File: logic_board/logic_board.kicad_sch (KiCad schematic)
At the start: 1 part

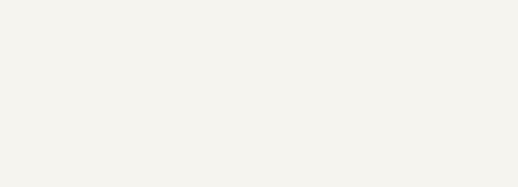
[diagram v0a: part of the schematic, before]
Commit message: Add headphone jack
Change PCB to proper size.
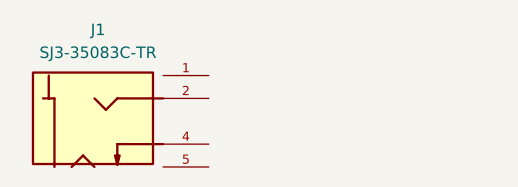
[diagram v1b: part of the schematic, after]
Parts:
- added J1: SJ3-35083C-TR, Custom_Footprints:SAMESKY_SJ3-35083C-TR, symbol Custom_Symbols:SJ3-35083C-TR
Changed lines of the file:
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@@
 	(paper "A4")
+	(symbol
+		(lib_id "Custom_Symbols:SJ3-35083C-TR")
+		(at 73.66 96.52 0)
+		(unit 1)
+		(exclude_from_sim no)
+		(in_bom yes)
+		(on_board yes)
+		(dnp no)
+		(fields_autoplaced yes)
+		(property "Reference" "J1"
+			(at 71.5134 86.36 0)
+			(effects
+				(font
+					(size 1.27 1.27)
+				)
+			)
+		)
+		(property "Value" "SJ3-35083C-TR"
+			(at 71.5134 88.9 0)
+			(effects
+				(font
+					(size 1.27 1.27)
+				)
+			)
+		)
+		(property "Footprint" "Custom_Footprints:SAMESKY_SJ3-35083C-TR"
+			(at 73.66 96.52 0)
+			(effects
+				(font
+					(size 1.27 1.27)
+				)
+				(justify bottom)
+				(hide yes)
+			)
+		)
+		(property "Datasheet" "https://www.sameskydevices.com/product/resource/sj3-3508x.pdf"
+			(at 73.66 96.52 0)
+			(effects
+				(font
+					(size 1.27 1.27)
+				)
+				(hide yes)
+			)
+		)
+		(property "Description" "3.5mm Audio Jack"
+			(at 73.66 96.52 0)
+			(effects
+				(font
+					(size 1.27 1.27)
+				)
+				(hide yes)
+			)
+		)
+		(property "PARTREV" "1.01"
+			(at 73.66 96.52 0)
+			(effects
+				(font
+					(size 1.27 1.27)
+				)
+				(justify bottom)
+				(hide yes)
+			)
+		)
+		(property "STANDARD" "Manufacturer Recommendations"
+			(at 73.66 96.52 0)
+			(effects
+				(font
+					(size 1.27 1.27)
+				)
+				(justify bottom)
+				(hide yes)
+			)
+		)
+		(property "MAXIMUM_PACKAGE_HEIGHT" "5.3mm"
+			(at 73.66 96.52 0)
+			(effects
+				(font
+					(size 1.27 1.27)
+				)
+				(justify bottom)
+				(hide yes)
+			)
+		)
+		(property "MANUFACTURER" "Same Sky"
+			(at 73.66 96.52 0)
+			(effects
+				(font
+					(size 1.27 1.27)
+				)
+				(justify bottom)
+				(hide yes)
+			)
+		)
+		(pin "1"
+		)
+		(pin "2"
+		)
+		(pin "4"
+		)
+		(pin "5"
+		)
+		(instances
+			(project ""
+				(path "/b7b37fe1-b409-497a-9440-d94d882f6459"
+					(reference "J1")
+					(unit 1)
+				)
+			)
+		)
+	)
 	(symbol
 		(lib_id "Device:R")

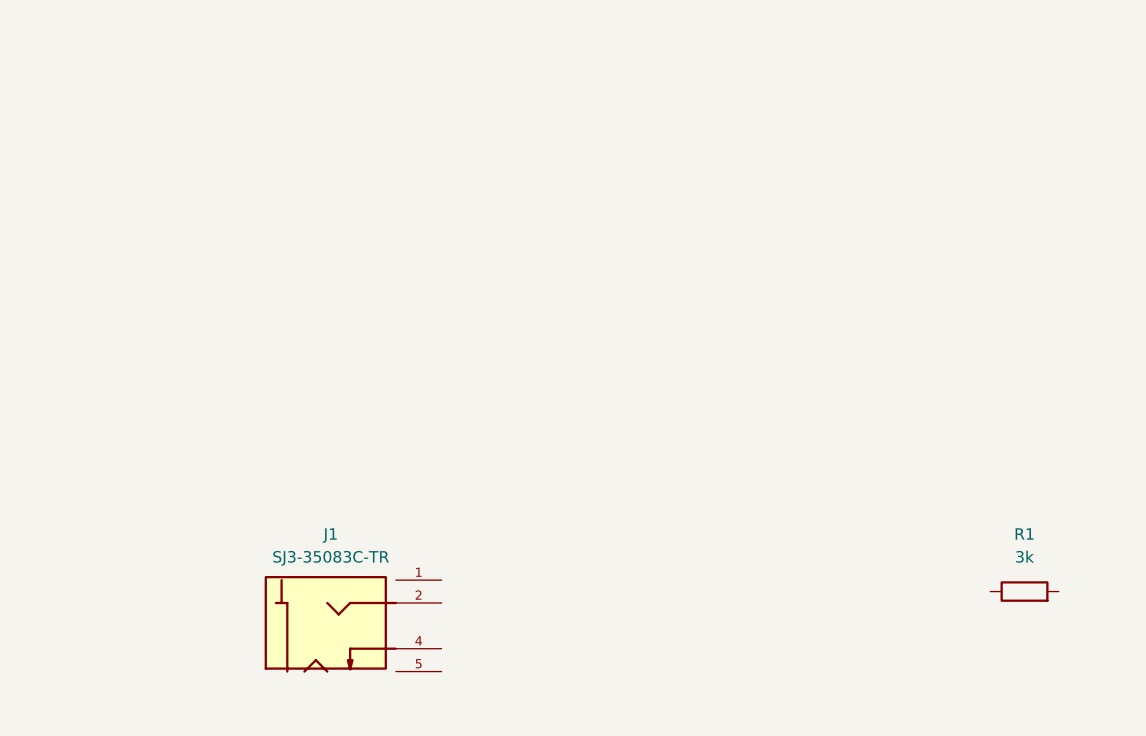
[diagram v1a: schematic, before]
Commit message: Component selection
Imported specific parts into KiCAD project library (including JLCPCB part numbers).
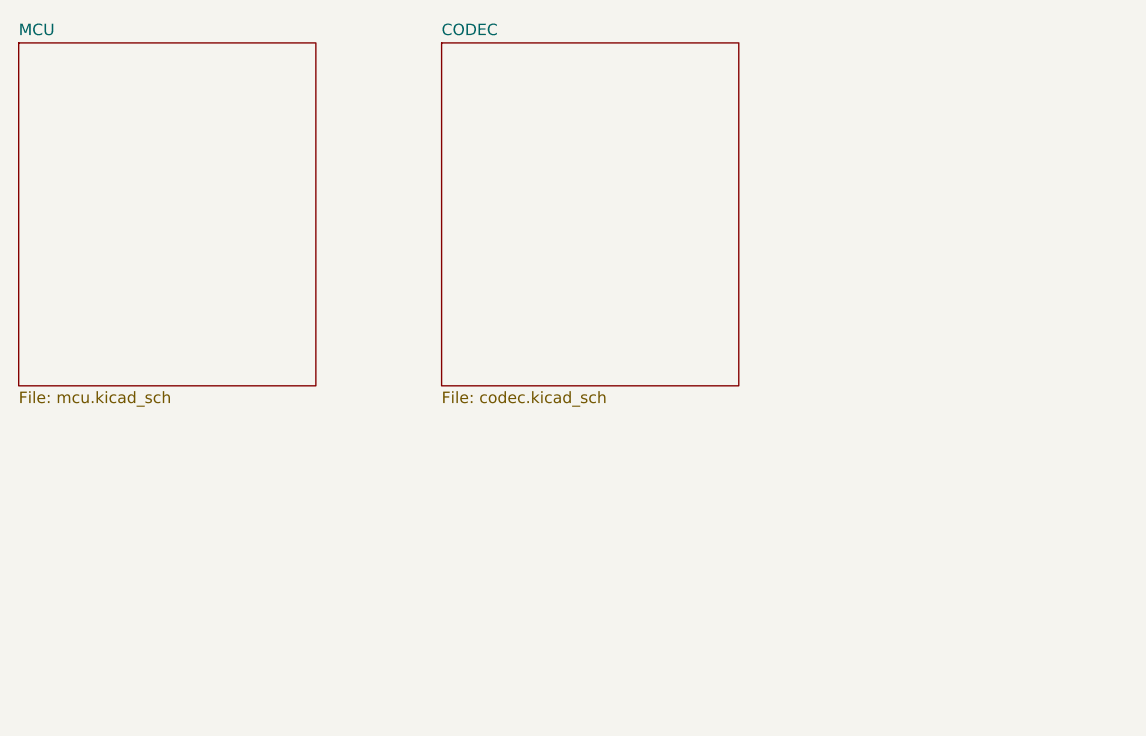
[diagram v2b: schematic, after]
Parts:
- removed J1: SJ3-35083C-TR, Custom_Footprints:SAMESKY_SJ3-35083C-TR, symbol Custom_Symbols:SJ3-35083C-TR
- removed R1: 3k, Resistor_SMD:R_0402_1005Metric, symbol Device:R
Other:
- added sheet CODEC (codec.kicad_sch)
- added sheet MCU (mcu.kicad_sch)
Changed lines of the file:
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@@
 	(generator_version "9.0")
 	(paper "A4")
-	(symbol
-		(lib_id "Custom_Symbols:SJ3-35083C-TR")
-		(at 73.66 96.52 0)
-		(unit 1)
+	(sheet
+		(at 83.82 31.75)
+		(size 33.02 38.1)
 		(exclude_from_sim no)
 		(in_bom yes)
@@
 		(dnp no)
 		(fields_autoplaced yes)
-		(property "Reference" "J1"
-			(at 71.5134 86.36 0)
+		(stroke
+			(width 0.1524)
+			(type solid)
+		)
+		(fill
+			(color 0 0 0 0.0000)
+		)
+		(property "Sheetname" "CODEC"
+			(at 83.82 31.0384 0)
 			(effects
 				(font
 					(size 1.27 1.27)
 				)
+				(justify left bottom)
 			)
 		)
-		(property "Value" "SJ3-35083C-TR"
-			(at 71.5134 88.9 0)
+		(property "Sheetfile" "codec.kicad_sch"
+			(at 83.82 70.4346 0)
 			(effects
 				(font
 					(size 1.27 1.27)
 				)
+				(justify left top)
 			)
 		)
-		(property "Footprint" "Custom_Footprints:SAMESKY_SJ3-35083C-TR"
-			(at 73.66 96.52 0)
-			(effects
-				(font
-					(size 1.27 1.27)
-				)
-				(justify bottom)
-				(hide yes)
-			)
-		)
-		(property "Datasheet" "https://www.sameskydevices.com/product/resource/sj3-3508x.pdf"
-			(at 73.66 96.52 0)
-			(effects
-				(font
-					(size 1.27 1.27)
-				)
-				(hide yes)
-			)
-		)
-		(property "Description" "3.5mm Audio Jack"
-			(at 73.66 96.52 0)
-			(effects
-				(font
-					(size 1.27 1.27)
-				)
-				(hide yes)
-			)
-		)
-		(property "PARTREV" "1.01"
-			(at 73.66 96.52 0)
-			(effects
-				(font
-					(size 1.27 1.27)
-				)
-				(justify bottom)
-				(hide yes)
-			)
-		)
-		(property "STANDARD" "Manufacturer Recommendations"
-			(at 73.66 96.52 0)
-			(effects
-				(font
-					(size 1.27 1.27)
-				)
-				(justify bottom)
-				(hide yes)
-			)
-		)
-		(property "MAXIMUM_PACKAGE_HEIGHT" "5.3mm"
-			(at 73.66 96.52 0)
-			(effects
-				(font
-					(size 1.27 1.27)
-				)
-				(justify bottom)
-				(hide yes)
-			)
-		)
-		(property "MANUFACTURER" "Same Sky"
-			(at 73.66 96.52 0)
-			(effects
-				(font
-					(size 1.27 1.27)
-				)
-				(justify bottom)
-				(hide yes)
-			)
-		)
-		(pin "1"
-		)
-		(pin "2"
-		)
-		(pin "4"
-		)
-		(pin "5"
-		)
 		(instances
-			(project ""
+			(project "logic_board"
 				(path "/b7b37fe1-b409-497a-9440-d94d882f6459"
-					(reference "J1")
-					(unit 1)
+					(page "3")
 				)
 			)
 		)
 	)
-	(symbol
-		(lib_id "Device:R")
-		(at 148.59 92.71 90)
-		(unit 1)
+	(sheet
+		(at 36.83 31.75)
+		(size 33.02 38.1)
 		(exclude_from_sim no)
 		(in_bom yes)
@@
 		(dnp no)
 		(fields_autoplaced yes)
-		(property "Reference" "R1"
-			(at 148.59 86.36 90)
+		(stroke
+			(width 0.1524)
+			(type solid)
+		)
+		(fill
+			(color 0 0 0 0.0000)
+		)
+		(property "Sheetname" "MCU"
+			(at 36.83 31.0384 0)
 			(effects
 				(font
 					(size 1.27 1.27)
 				)
+				(justify left bottom)
 			)
 		)
-		(property "Value" "3k"
-			(at 148.59 88.9 90)
+		(property "Sheetfile" "mcu.kicad_sch"
+			(at 36.83 70.4346 0)
 			(effects
 				(font
 					(size 1.27 1.27)
 				)
+				(justify left top)
 			)
 		)
-		(property "Footprint" "Resistor_SMD:R_0402_1005Metric"
-			(at 148.59 94.488 90)
-			(effects
-				(font
-					(size 1.27 1.27)
-				)
-				(hide yes)
-			)
-		)
-		(property "Datasheet" "~"
-			(at 148.59 92.71 0)
-			(effects
-				(font
-					(size 1.27 1.27)
-				)
-				(hide yes)
-			)
-		)
-		(property "Description" "Resistor"
-			(at 148.59 92.71 0)
-			(effects
-				(font
-					(size 1.27 1.27)
-				)
-				(hide yes)
-			)
-		)
-		(property "LCSC Part Number" "C4211"
-			(at 148.59 92.71 90)
-			(effects
-				(font
-					(size 1.27 1.27)
-				)
-				(hide yes)
-			)
-		)
-		(pin "2"
-		)
-		(pin "1"
-		)
 		(instances
-			(project ""
+			(project "logic_board"
 				(path "/b7b37fe1-b409-497a-9440-d94d882f6459"
-					(reference "R1")
-					(unit 1)
+					(page "2")
 				)
 			)

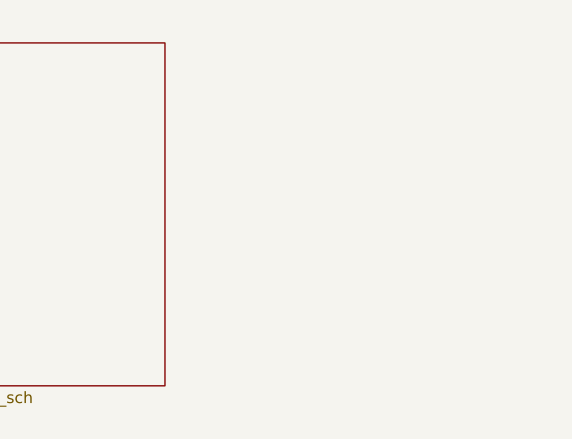
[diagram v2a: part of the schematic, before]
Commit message: Ready for routing. - Lay out all components in proper positions - Add all support passives (bypass caps, etc) - Add board corner cutouts for enclosure bosses.
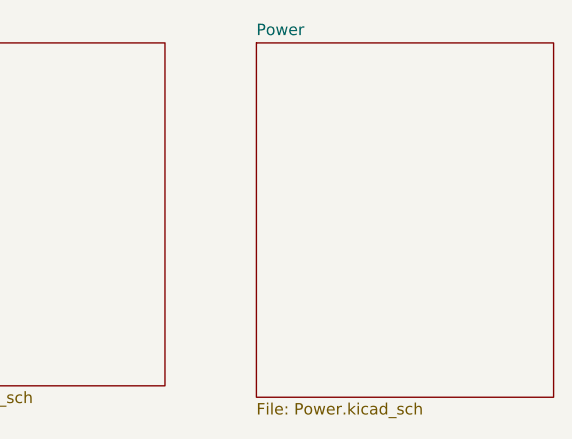
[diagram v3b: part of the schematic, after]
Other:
- added sheet Power (Power.kicad_sch)
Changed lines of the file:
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@@
 	(paper "A4")
+	(sheet
+		(at 127 31.75)
+		(size 33.02 39.37)
+		(exclude_from_sim no)
+		(in_bom yes)
+		(on_board yes)
+		(dnp no)
+		(fields_autoplaced yes)
+		(stroke
+			(width 0.1524)
+			(type solid)
+		)
+		(fill
+			(color 0 0 0 0.0000)
+		)
+		(property "Sheetname" "Power"
+			(at 127 31.0384 0)
+			(effects
+				(font
+					(size 1.27 1.27)
+				)
+				(justify left bottom)
+			)
+		)
+		(property "Sheetfile" "Power.kicad_sch"
+			(at 127 71.7046 0)
+			(effects
+				(font
+					(size 1.27 1.27)
+				)
+				(justify left top)
+			)
+		)
+		(instances
+			(project "logic_board"
+				(path "/b7b37fe1-b409-497a-9440-d94d882f6459"
+					(page "4")
+				)
+			)
+		)
+	)
 	(sheet
 		(at 83.82 31.75)

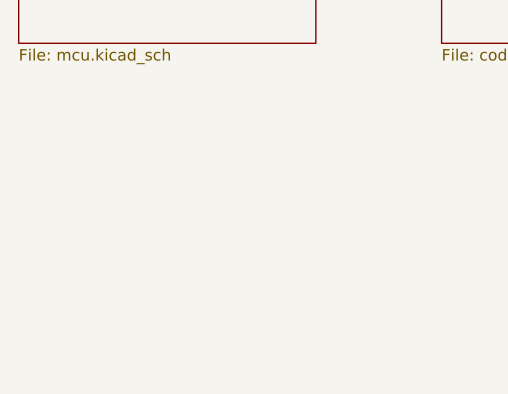
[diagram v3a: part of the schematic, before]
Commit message: Add fiducials take 2
Need to add to schematic so they don't get deleted with updating PCB from
schematic.
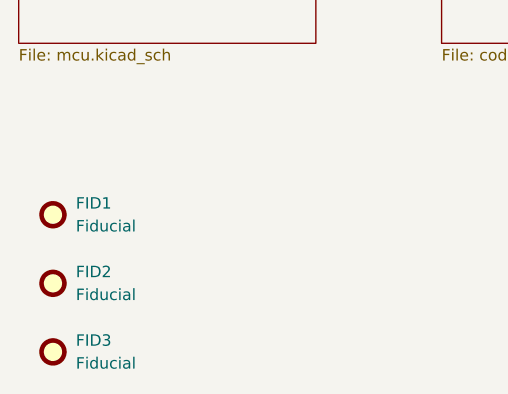
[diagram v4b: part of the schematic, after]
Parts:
- added FID1, FID2, FID3: Fiducial, Fiducial:Fiducial_0.5mm_Mask1mm, symbol Mechanical:Fiducial
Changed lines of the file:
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@@
 	(generator_version "9.0")
 	(paper "A4")
+	(symbol
+		(lib_id "Mechanical:Fiducial")
+		(at 40.64 104.14 0)
+		(unit 1)
+		(exclude_from_sim no)
+		(in_bom no)
+		(on_board yes)
+		(dnp no)
+		(fields_autoplaced yes)
+		(property "Reference" "FID3"
+			(at 43.18 102.8699 0)
+			(effects
+				(font
+					(size 1.27 1.27)
+				)
+				(justify left)
+			)
+		)
+		(property "Value" "Fiducial"
+			(at 43.18 105.4099 0)
+			(effects
+				(font
+					(size 1.27 1.27)
+				)
+				(justify left)
+			)
+		)
+		(property "Footprint" "Fiducial:Fiducial_0.5mm_Mask1mm"
+			(at 40.64 104.14 0)
+			(effects
+				(font
+					(size 1.27 1.27)
+				)
+				(hide yes)
+			)
+		)
+		(property "Datasheet" "~"
+			(at 40.64 104.14 0)
+			(effects
+				(font
+					(size 1.27 1.27)
+				)
+				(hide yes)
+			)
+		)
+		(property "Description" "Fiducial Marker"
+			(at 40.64 104.14 0)
+			(effects
+				(font
+					(size 1.27 1.27)
+				)
+				(hide yes)
+			)
+		)
+		(instances
+			(project "logic_board"
+				(path "/b7b37fe1-b409-497a-9440-d94d882f6459"
+					(reference "FID3")
+					(unit 1)
+				)
+			)
+		)
+	)
+	(symbol
+		(lib_id "Mechanical:Fiducial")
+		(at 40.64 96.52 0)
+		(unit 1)
+		(exclude_from_sim no)
+		(in_bom no)
+		(on_board yes)
+		(dnp no)
+		(fields_autoplaced yes)
+		(property "Reference" "FID2"
+			(at 43.18 95.2499 0)
+			(effects
+				(font
+					(size 1.27 1.27)
+				)
+				(justify left)
+			)
+		)
+		(property "Value" "Fiducial"
+			(at 43.18 97.7899 0)
+			(effects
+				(font
+					(size 1.27 1.27)
+				)
+				(justify left)
+			)
+		)
+		(property "Footprint" "Fiducial:Fiducial_0.5mm_Mask1mm"
+			(at 40.64 96.52 0)
+			(effects
+				(font
+					(size 1.27 1.27)
+				)
+				(hide yes)
+			)
+		)
+		(property "Datasheet" "~"
+			(at 40.64 96.52 0)
+			(effects
+				(font
+					(size 1.27 1.27)
+				)
+				(hide yes)
+			)
+		)
+		(property "Description" "Fiducial Marker"
+			(at 40.64 96.52 0)
+			(effects
+				(font
+					(size 1.27 1.27)
+				)
+				(hide yes)
+			)
+		)
+		(instances
+			(project "logic_board"
+				(path "/b7b37fe1-b409-497a-9440-d94d882f6459"
+					(reference "FID2")
+					(unit 1)
+				)
+			)
+		)
+	)
+	(symbol
+		(lib_id "Mechanical:Fiducial")
+		(at 40.64 88.9 0)
+		(unit 1)
+		(exclude_from_sim no)
+		(in_bom no)
+		(on_board yes)
+		(dnp no)
+		(fields_autoplaced yes)
+		(property "Reference" "FID1"
+			(at 43.18 87.6299 0)
+			(effects
+				(font
+					(size 1.27 1.27)
+				)
+				(justify left)
+			)
+		)
+		(property "Value" "Fiducial"
+			(at 43.18 90.1699 0)
+			(effects
+				(font
+					(size 1.27 1.27)
+				)
+				(justify left)
+			)
+		)
+		(property "Footprint" "Fiducial:Fiducial_0.5mm_Mask1mm"
+			(at 40.64 88.9 0)
+			(effects
+				(font
+					(size 1.27 1.27)
+				)
+				(hide yes)
+			)
+		)
+		(property "Datasheet" "~"
+			(at 40.64 88.9 0)
+			(effects
+				(font
+					(size 1.27 1.27)
+				)
+				(hide yes)
+			)
+		)
+		(property "Description" "Fiducial Marker"
+			(at 40.64 88.9 0)
+			(effects
+				(font
+					(size 1.27 1.27)
+				)
+				(hide yes)
+			)
+		)
+		(instances
+			(project ""
+				(path "/b7b37fe1-b409-497a-9440-d94d882f6459"
+					(reference "FID1")
+					(unit 1)
+				)
+			)
+		)
+	)
 	(sheet
 		(at 127 31.75)

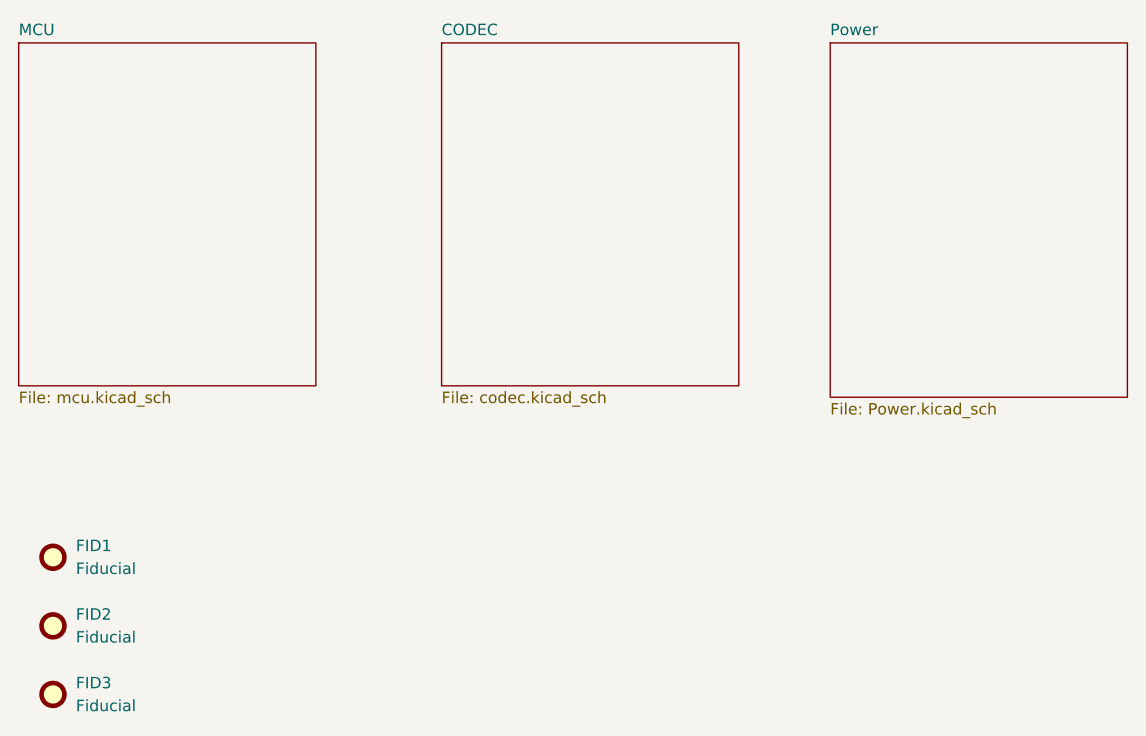
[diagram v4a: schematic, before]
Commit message: Minor cosmetic tweaks, fix silkscreen references
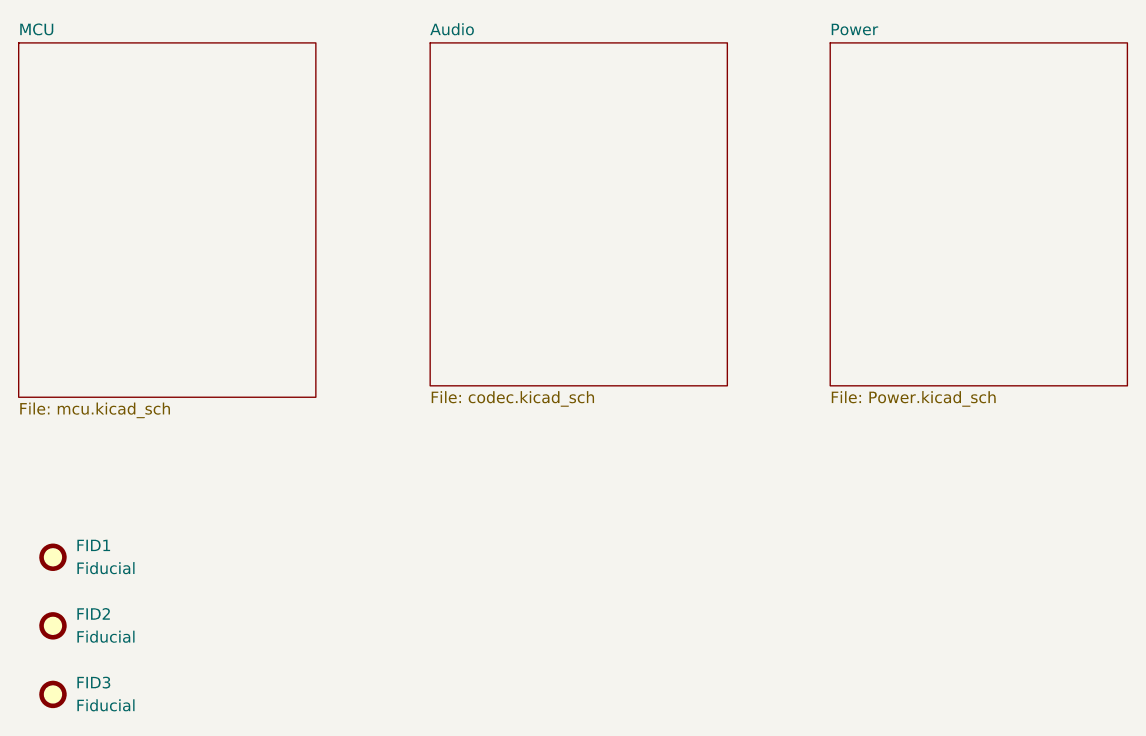
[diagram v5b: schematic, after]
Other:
- sheet CODEC renamed Audio
- title: (none) -> Headphone Guitar Practice Amp
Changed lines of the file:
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@@
 	(generator_version "9.0")
 	(paper "A4")
+	(title_block
+		(title "Headphone Guitar Practice Amp")
+		(date "2026-01-02")
+		(rev "2.0")
+	)
 	(symbol
 		(lib_id "Mechanical:Fiducial")
@@
 	(sheet
 		(at 127 31.75)
-		(size 33.02 39.37)
+		(size 33.02 38.1)
 		(exclude_from_sim no)
 		(in_bom yes)
@@
 		)
 		(property "Sheetfile" "Power.kicad_sch"
-			(at 127 71.7046 0)
+			(at 127 70.4346 0)
 			(effects
 				(font
@@
 	)
 	(sheet
-		(at 83.82 31.75)
+		(at 82.55 31.75)
 		(size 33.02 38.1)
 		(exclude_from_sim no)
@@
 			(color 0 0 0 0.0000)
 		)
-		(property "Sheetname" "CODEC"
-			(at 83.82 31.0384 0)
+		(property "Sheetname" "Audio"
+			(at 82.55 31.0384 0)
 			(effects
 				(font
@@
 		)
 		(property "Sheetfile" "codec.kicad_sch"
-			(at 83.82 70.4346 0)
+			(at 82.55 70.4346 0)
 			(effects
 				(font
@@
 	(sheet
 		(at 36.83 31.75)
-		(size 33.02 38.1)
+		(size 33.02 39.37)
 		(exclude_from_sim no)
 		(in_bom yes)
@@
 		)
 		(property "Sheetfile" "mcu.kicad_sch"
-			(at 36.83 70.4346 0)
-			(effects
-				(font
+			(at 36.83 71.7046 0)
+			(effects
+				(font
